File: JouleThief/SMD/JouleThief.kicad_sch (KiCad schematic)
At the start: 14 parts, among them J1 Screw_Terminal_01x02, J2 Screw_Terminal_01x02, Q1 BC547, Q2 BC547

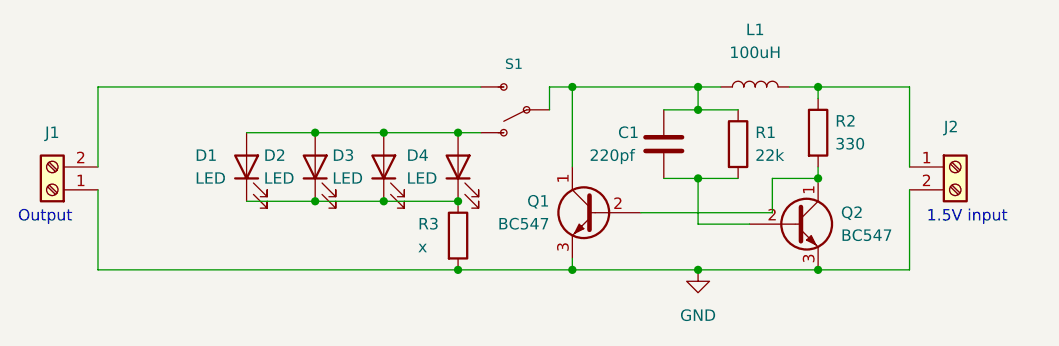
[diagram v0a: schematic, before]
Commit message: Updated Joule thief schematic values
Inductor: 220uH
Capacitor: 100pF
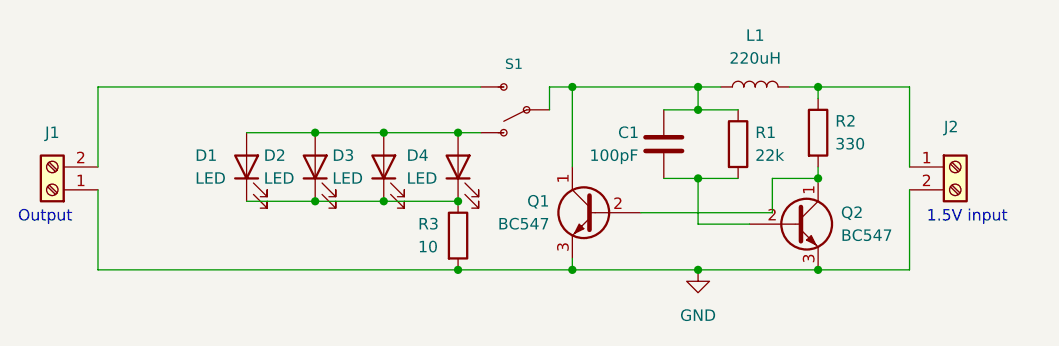
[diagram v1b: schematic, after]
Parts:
- C1: value 220pf -> 100pF
- L1: value 100uH -> 220uH
- R3: value x -> 10
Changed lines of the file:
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@@
   (symbol (lib_id "Device:L") (at 158.115 90.805 90) (unit 1)
     (in_bom yes) (on_board yes) (fields_autoplaced)
-    (property "Reference" "L1" (id 0) (at 158.115 84.455 90))
-    (property "Value" "100uH" (id 1) (at 158.115 86.995 90))
+    (property "Reference" "L1" (id 0) (at 158.115 85.09 90))
+    (property "Value" "220uH" (id 1) (at 158.115 87.63 90))
     (property "Footprint" "Inductor_SMD:L_6.3x6.3_H3" (id 2) (at 158.115 90.805 0)
       (effects (font (size 1.27 1.27)) hide)
@@
       (effects (font (size 1.27 1.27)) (justify left))
     )
-    (property "Value" "220pf" (id 1) (at 139.7 98.425 0)
+    (property "Value" "100pF" (id 1) (at 139.7 98.425 0)
       (effects (font (size 1.27 1.27)) (justify left))
     )
@@
       (effects (font (size 1.27 1.27)) (justify left))
     )
-    (property "Value" "x" (id 1) (at 120.65 108.585 0)
+    (property "Value" "10" (id 1) (at 120.65 108.585 0)
       (effects (font (size 1.27 1.27)) (justify left))
     )
@@
     )
     (path "/56f57a0c-d952-4b14-b499-4833f5f6a321"
-      (reference "C1") (unit 1) (value "220pf") (footprint "Capacitor_SMD:C_0805_2012Metric_Pad1.18x1.45mm_HandSolder")
+      (reference "C1") (unit 1) (value "100pF") (footprint "Capacitor_SMD:C_0805_2012Metric_Pad1.18x1.45mm_HandSolder")
     )
     (path "/a3379bb9-2fa5-4298-a436-0e0faa7bcb5e"
@@
     )
     (path "/41c982a7-98bb-4b69-93c8-cae707855073"
-      (reference "L1") (unit 1) (value "100uH") (footprint "Inductor_SMD:L_6.3x6.3_H3")
+      (reference "L1") (unit 1) (value "220uH") (footprint "Inductor_SMD:L_6.3x6.3_H3")
     )
     (path "/473a4415-2386-4149-a3fe-7889d826e6e0"
@@
     )
     (path "/fec27d13-0747-41e3-a4d8-e21a45052ada"
-      (reference "R3") (unit 1) (value "x") (footprint "Resistor_SMD:R_0805_2012Metric_Pad1.20x1.40mm_HandSolder")
+      (reference "R3") (unit 1) (value "10") (footprint "Resistor_SMD:R_0805_2012Metric_Pad1.20x1.40mm_HandSolder")
     )
     (path "/5a60103d-c1f5-44fb-9ca6-bd09329bef56"
